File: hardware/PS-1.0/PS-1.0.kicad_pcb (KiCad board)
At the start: 2 copper layers, 119.7 x 199.4 mm, 48 parts, among them J1 PinSocket_02x16_P2.54mm_Verti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, J2 Conn_01x05, J3 Conn_01x05, J8 Conn_01x03, J9 Conn_01x03, K1 RAYEX-L90, K2 RAYEX-L90, Q1 IRFPE50, Q2 IRFPE50, Q3 IRFPE50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

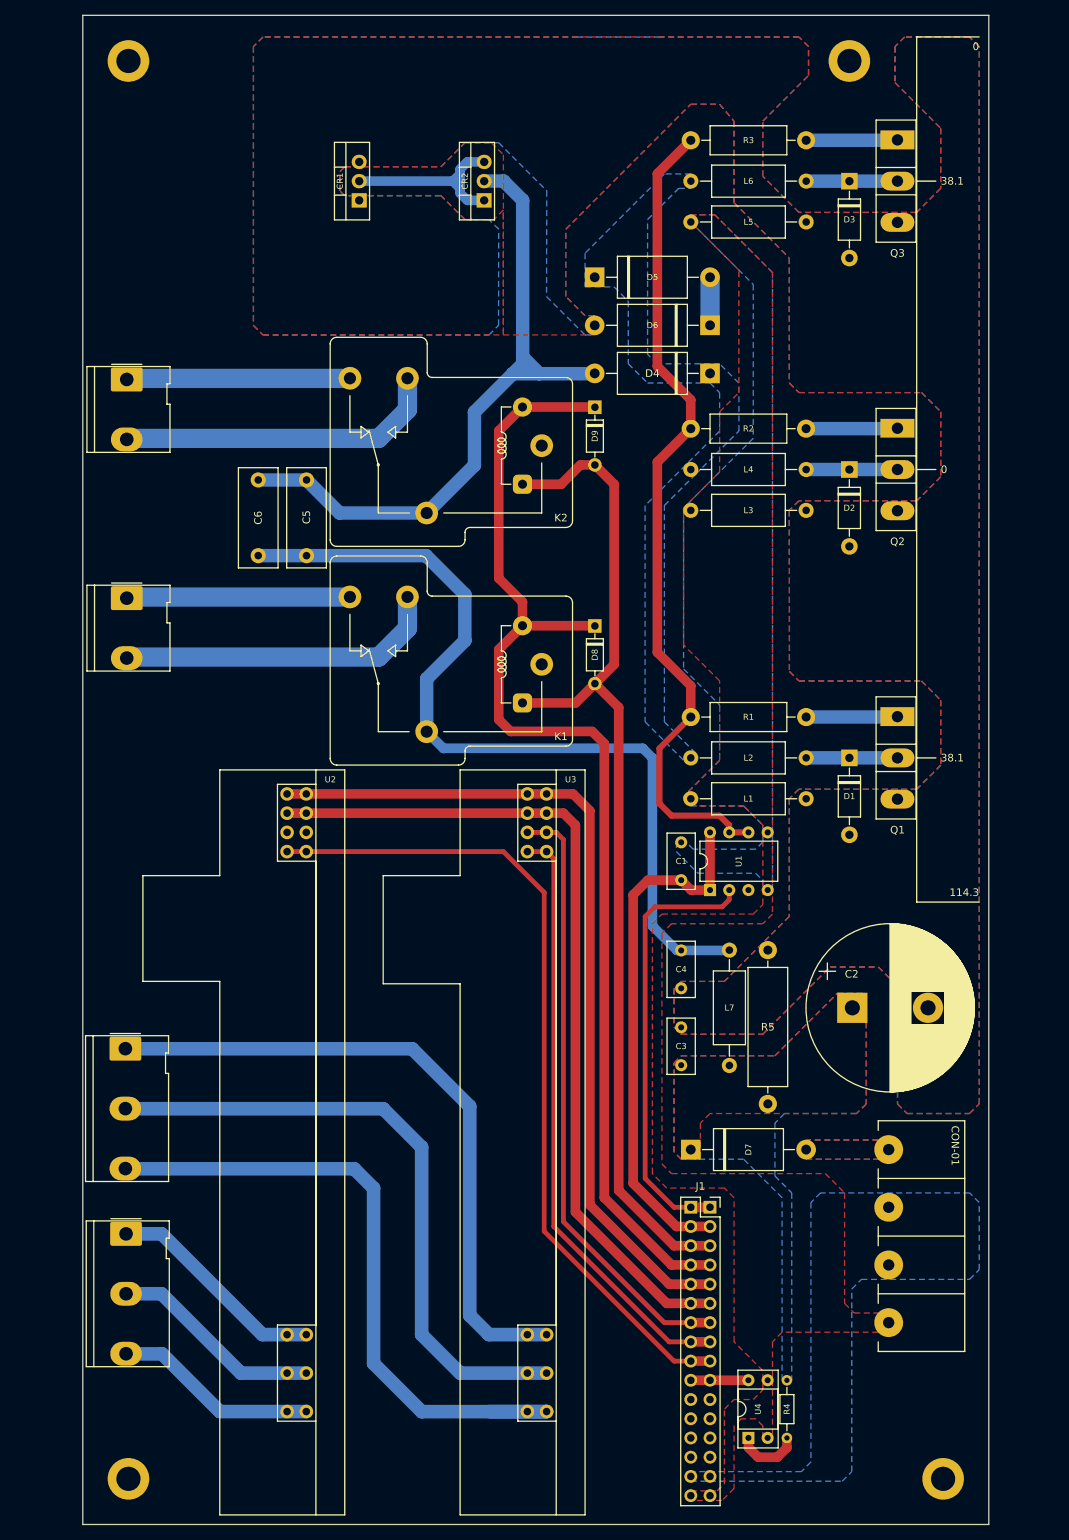
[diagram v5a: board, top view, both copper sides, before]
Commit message: modified:   .DS_Store 	modified:   BoM.xlsx 	modified:   hardware/MSD-1.0/MSD-1.0-B_Cu.gbr 	modified:   hardware/MSD-1.0/MSD-1.0-B_Mask.gbr 	modified:   hardware/MSD-1.0/MSD-1.0-B_Paste.gbr 	modified:   hardware/MSD-1.0/MSD-1.0-B_Silkscreen.gbr 	modified:   hardware/MSD-1.0/MSD-1.0-Edge_Cuts.gbr 	modified:   hardware/MSD-1.0/MSD-1.0-F_Cu.gbr 	modified:   hardware/MSD-1.0/MSD-1.0-F_Mask.gbr 	modified:   hardware/MSD-1.0/MSD-1.0-F_Paste.gbr 	modified:   hardware/MSD-1.0/MSD-1.0-F_Silkscreen.gbr 	modified:   hardware/MSD-1.0/MSD-1.0-NPTH.drl 	modified:   hardware/MSD-1.0/MSD-1.0-PTH.drl 	deleted:    hardware/MSD-1.0/MSD-1.0-backups/MSD-1.0-2025-04-08_105747.zip 	new file:   hardware/MSD-1.0/MSD-1.0-backups/MSD-1.0-2025-04-29_135016.zip 	modified:   hardware/MSD-1.0/MSD-1.0-job.gbrjob 	modified:   hardware/MSD-1.0/MSD-1.zip 	new file:   hardware/PS-1.0/PS-1.0-B_Cu.gbr 	new file:   hardware/PS-1.0/PS-1.0-B_Mask.gbr 	new file:   hardware/PS-1.0/PS-1.0-B_Paste.gbr 	new file:   hardware/PS-1.0/PS-1.0-B_Silkscreen.gbr 	new file:   hardware/PS-1.0/PS-1.0-Edge_Cuts.gbr 	new file:   hardware/PS-1.0/PS-1.0-F_Cu.gbr 	new file:   hardware/PS-1.0/PS-1.0-F_Mask.gbr 	new file:   hardware/PS-1.0/PS-1.0-F_Paste.gbr 	new file:   hardware/PS-1.0/PS-1.0-F_Silkscreen.gbr 	new file:   hardware/PS-1.0/PS-1.0-NPTH.drl 	new file:   hardware/PS-1.0/PS-1.0-PTH.drl 	deleted:    hardware/PS-1.0/PS-1.0-backups/PS-1.0-2025-04-11_131644.zip 	deleted:    hardware/PS-1.0/PS-1.0-backups/PS-1.0-2025-04-14_085622.zip 	deleted:    hardware/PS-1.0/PS-1.0-backups/PS-1.0-2025-04-14_104133.zip 	deleted:    hardware/PS-1.0/PS-1.0-backups/PS-1.0-2025-04-14_105043.zip 	deleted:    hardware/PS-1.0/PS-1.0-backups/PS-1.0-2025-04-14_110044.zip 	deleted:    hardware/PS-1.0/PS-1.0-backups/PS-1.0-2025-04-16_155906.zip 	deleted:    hardware/PS-1.0/PS-1.0-backups/PS-1.0-2025-04-16_160456.zip 	new file:   hardware/PS-1.0/PS-1.0-backups/PS-1.0-2025-04-29_112020.zip 	new file:   hardware/PS-1.0/PS-1.0-backups/PS-1.0-2025-04-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
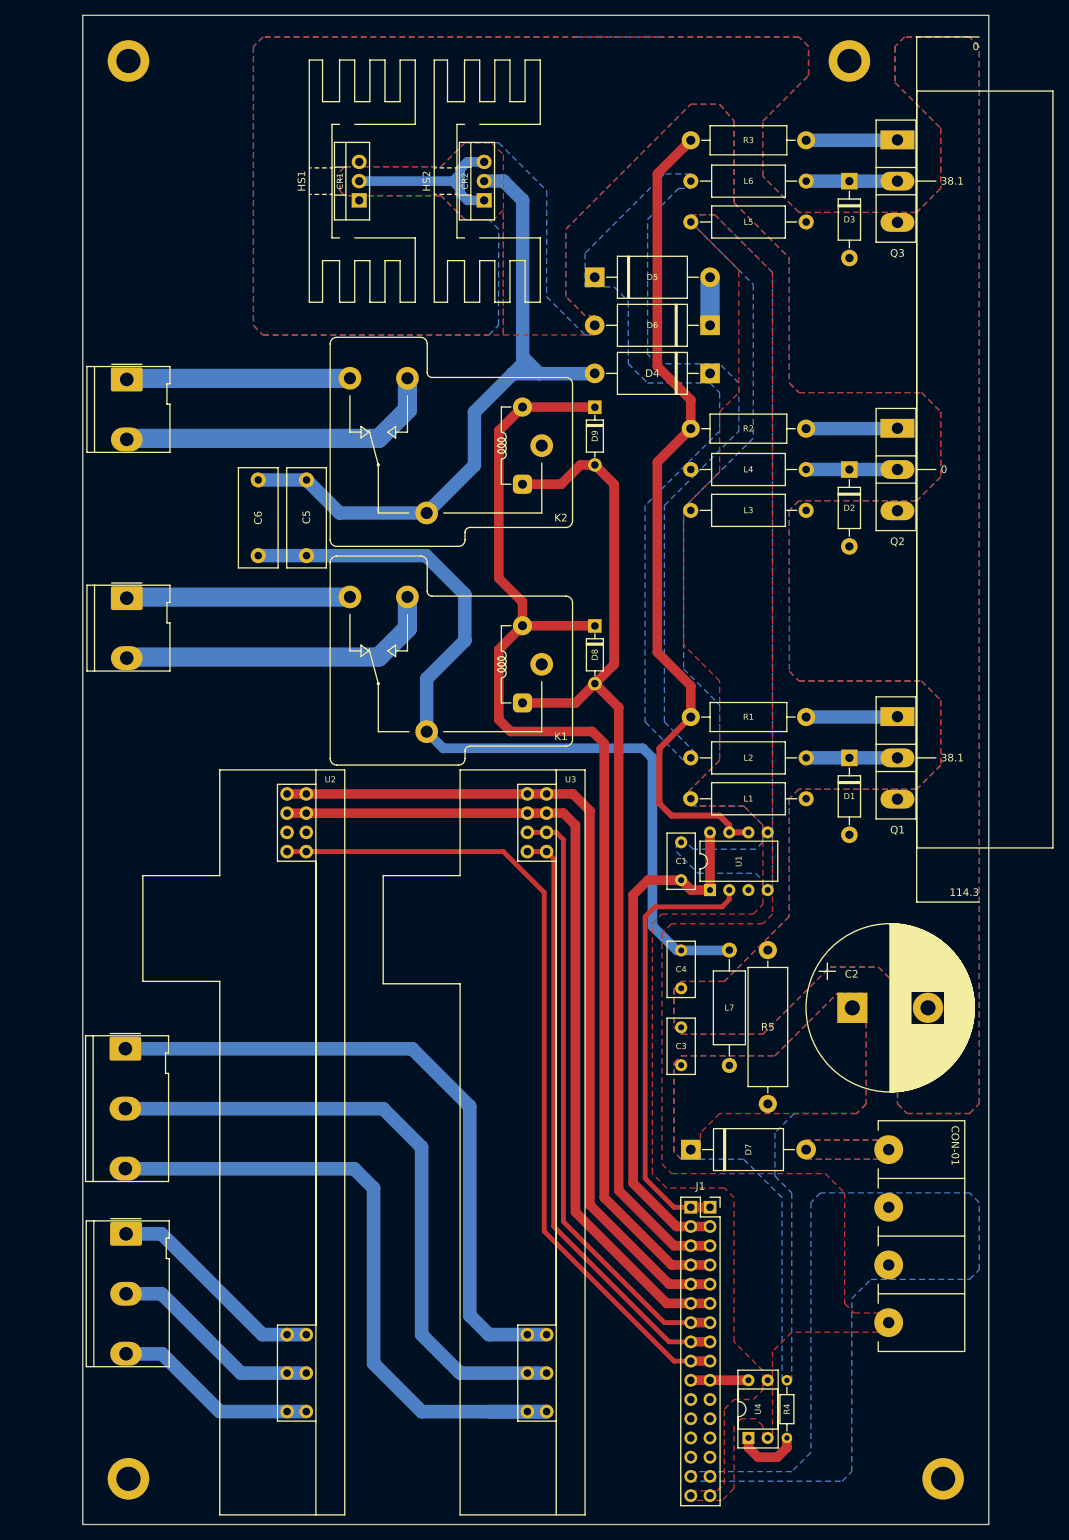
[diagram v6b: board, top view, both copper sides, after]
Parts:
- added HS1: Heatsink, Heatsink:Heatsink_Stonecold_HS-132_32x14mm_2xFixation1.5mm_NoPad, F.Cu at (155.6, 51.1)
- added HS2: Heatsink, Heatsink:Heatsink_Stonecold_HS-132_32x14mm_2xFixation1.5mm_NoPad, F.Cu at (172.1, 51.1)
- added HS3: Heatsink, Heatsink:Heatsink_Custom_10x18x50, F.Cu at (230.8, 89.2)
